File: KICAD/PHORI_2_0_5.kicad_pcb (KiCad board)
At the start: 2 copper layers, 125 x 80.9 mm, 114 parts, among them J1 Conn_01x06_Female, J2 Conn_01x02, J2 Conn_01x04_Female, J4 Conn_01x01, J4 Conn_01x04_Male, J5 Rumble, J6 PinSocket_1x04_P2.00mm_Vertic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, J9 USB_B_Micro, Q1 Q_NMOS_GSD, Q2 Q_PMOS_GDS, Q3 Q_NMOS_GSD, SW1 A, SW10 Dup, SW11 Dright, SW2 B, SW4 Y, SW5 Start, SW6 L, SW7 R, SW8 Z, U1 MCP3002, U10 DRV5055Z3QDBZT, U11 DRV5055Z3QDBZT, U12 USBLC6-2P6, U13 USBLC6-2P6, U2 Stickbox_Assembly_Main, U3 DRV5055Z3QDBZT, U4 DRV5055Z3QDBZT, U5 Stickbox_Assembly, U6 AMS1117-3.3, U7 W25Q128JVS, U8 RP2040, Y1 Crystal_GND24

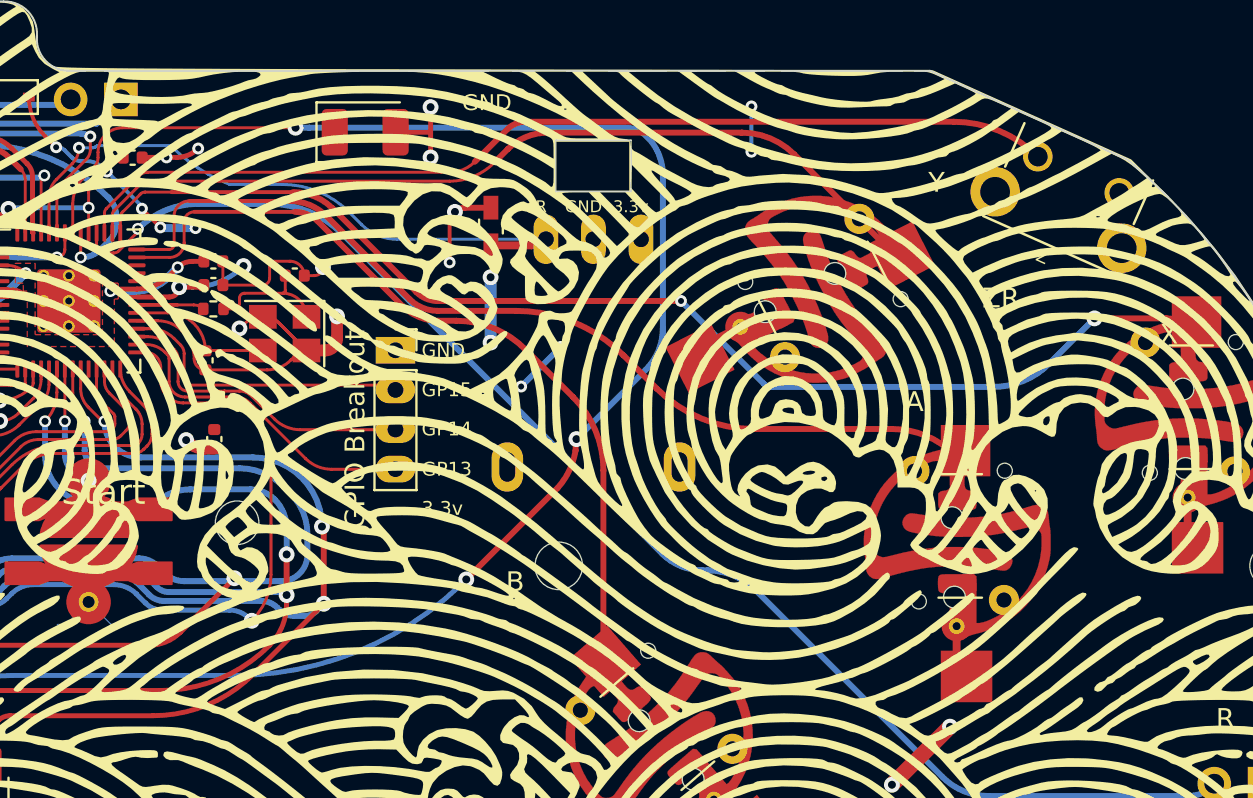
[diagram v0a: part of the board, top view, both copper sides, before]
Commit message: GND on Rp2040
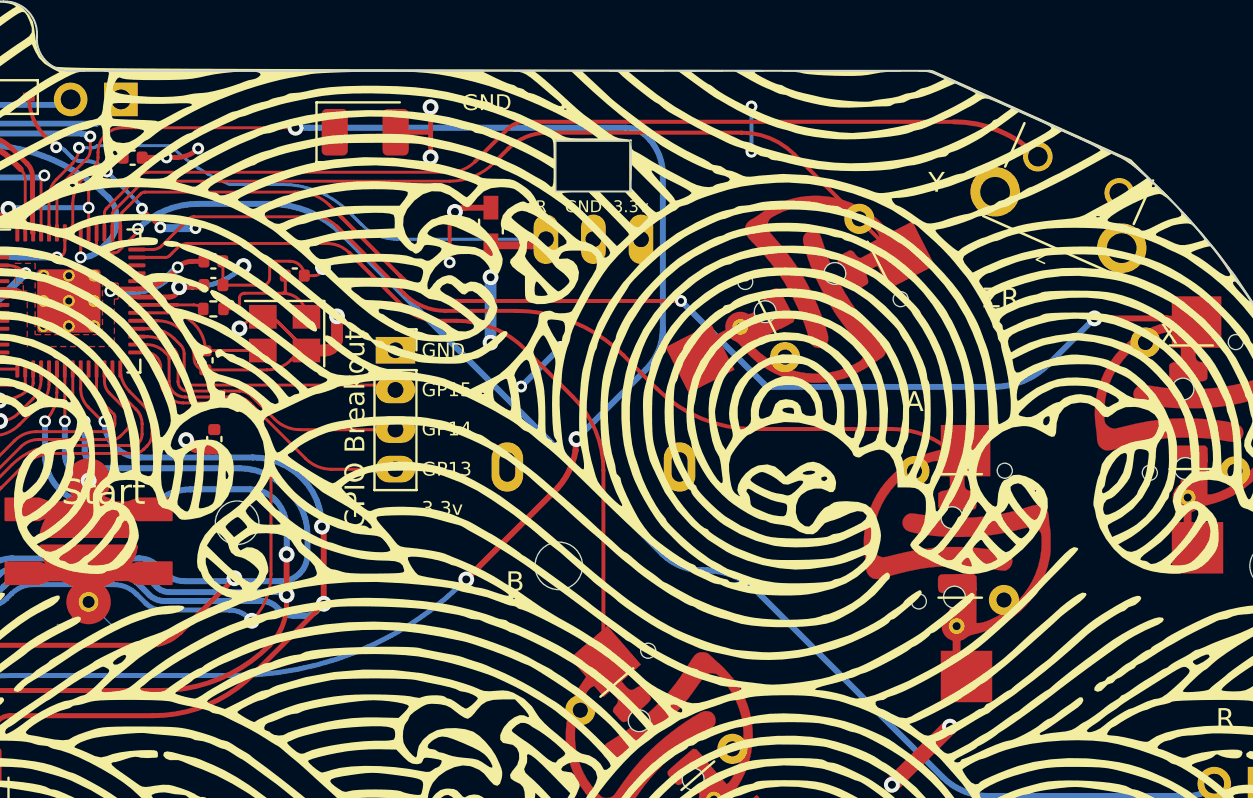
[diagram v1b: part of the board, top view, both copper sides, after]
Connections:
- U8 pad 57: (no net) -> GND
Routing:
- net B: track 42.1 -> 39.5 mm
- net A: track 47.4 -> 45.8 mm
- added copper zone on F.Cu, net +1V1
- removed copper zone on F.Cu, net (none)
